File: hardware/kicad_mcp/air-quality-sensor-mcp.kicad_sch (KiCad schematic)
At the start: 16 parts, among them J1 JST_PH_2pin_Battery, U1 XIAO_ESP32C3, U2 Adafruit_SCD41, U3 Adafruit_SGP41, U4 SSD1306_OLED_128x64, U5 TP4056_USB-C_Module

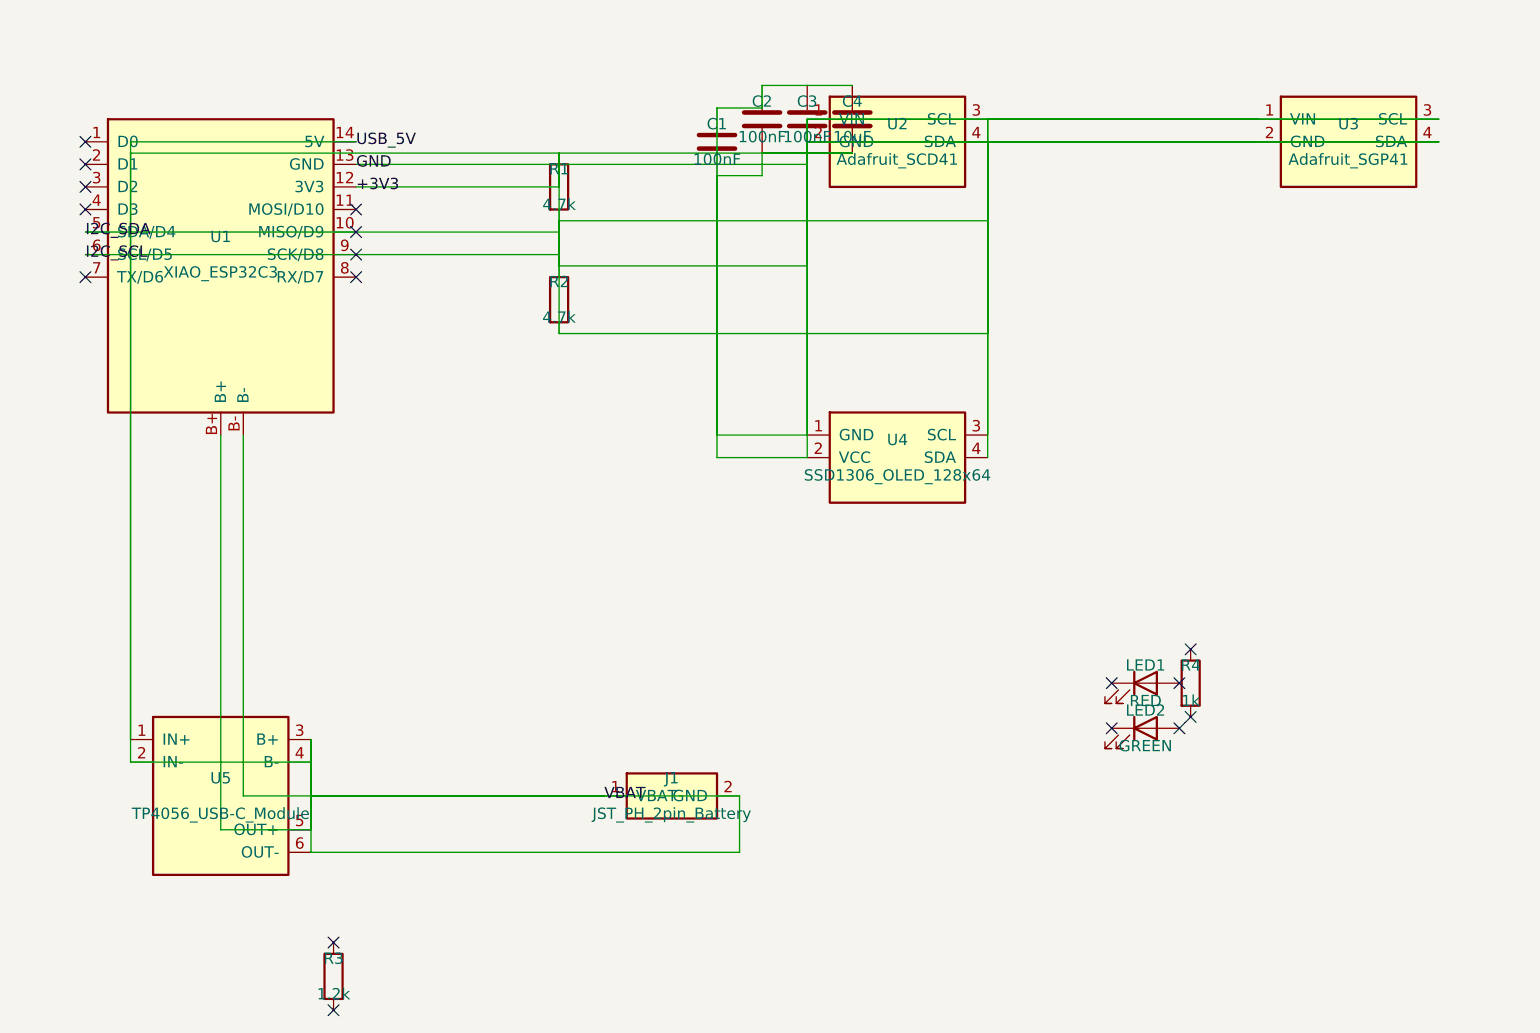
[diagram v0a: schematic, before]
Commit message: Rewire MCP schematic visibly and refresh hardware docs
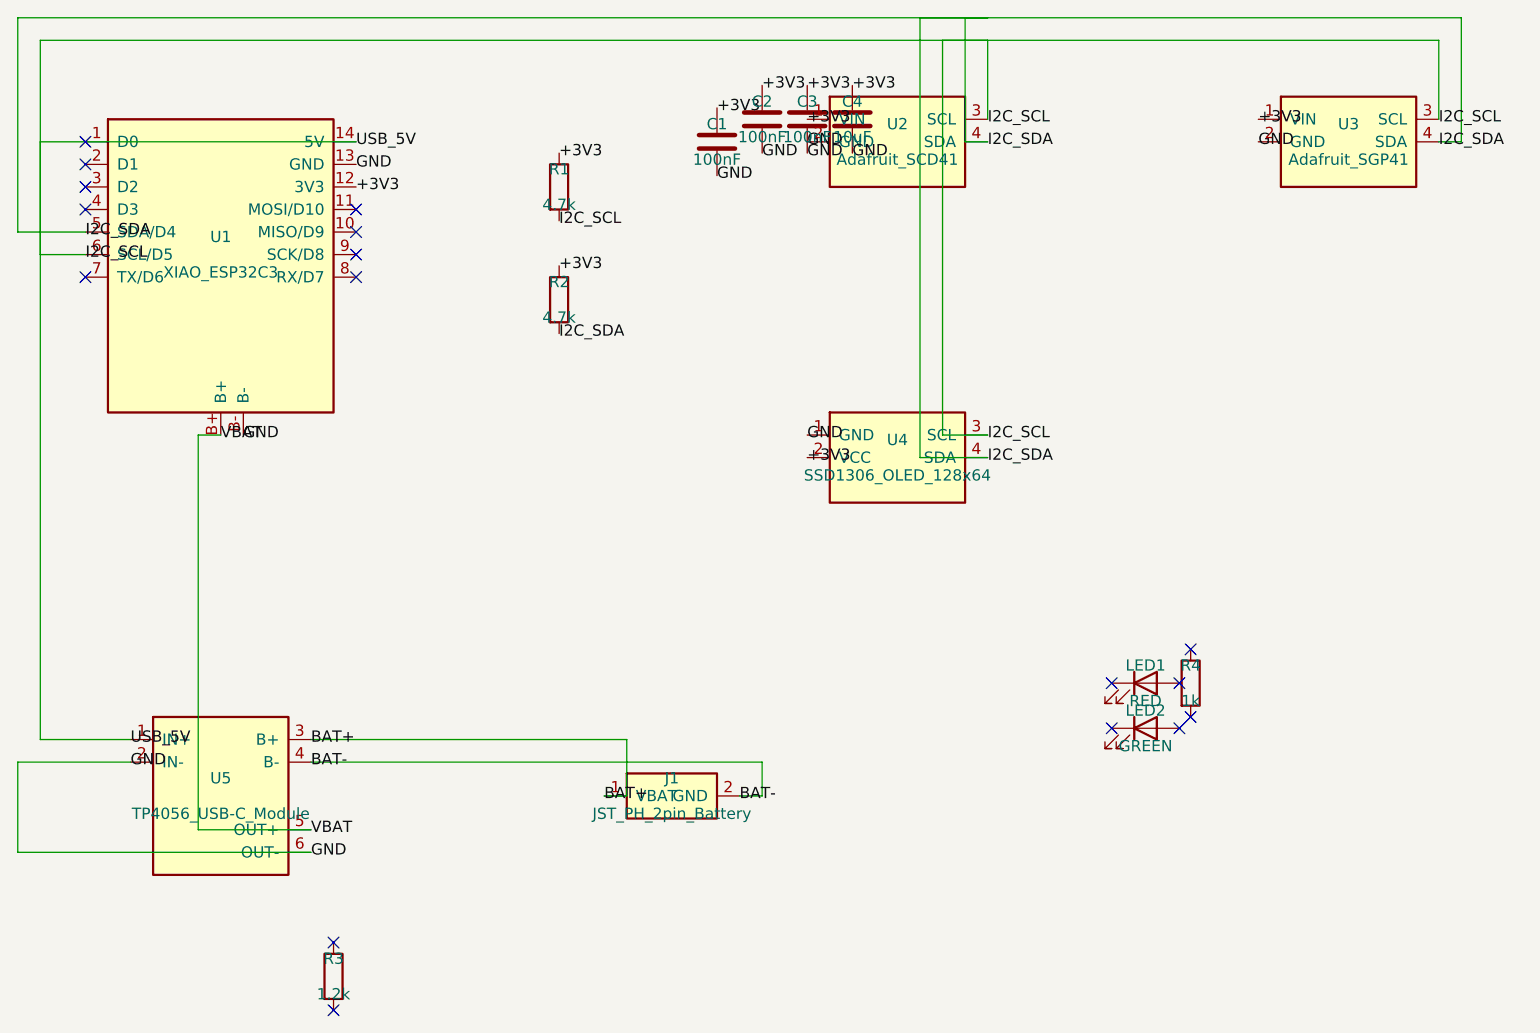
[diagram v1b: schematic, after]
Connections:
- net +3V3: no longer C1.2, C2.2, C3.2, C4.2, J1.1 (VBAT), J1.2 (GND), R1.2, R2.2, U1.13 (GND), U1.14 (5V), U1.5 (SDA/D4), U1.6 (SCL/D5), U1.B+, U1.B-, U2.2 (GND), U2.3 (SCL), U2.4 (SDA), U3.2 (GND), U3.3 (SCL), U3.4 (SDA), U4.1 (GND), U4.3 (SCL), U4.4 (SDA), U5.1 (IN+), U5.2 (IN-), U5.3 (B+), U5.4 (B-), U5.5 (OUT+), U5.6 (OUT-)
- new net BAT+: J1.1 (VBAT), U5.3 (B+)
- new net BAT-: J1.2 (GND), U5.4 (B-)
- new net GND: C1.2, C2.2, C3.2, C4.2, U1.13 (GND), U1.B-, U2.2 (GND), U3.2 (GND), U4.1 (GND), U5.2 (IN-), U5.6 (OUT-)
- new net I2C_SCL: R1.2, U1.14 (5V), U1.6 (SCL/D5), U2.3 (SCL), U3.3 (SCL), U4.3 (SCL), U5.1 (IN+)
- new net I2C_SDA: R2.2, U1.5 (SDA/D4), U2.4 (SDA), U3.4 (SDA), U4.4 (SDA)
- new net VBAT: U1.B+, U5.5 (OUT+)
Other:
- title: Wearable Air Quality Sensor (Fresh MCP Design) -> Wearable Air Quality Sensor (MCP Design)

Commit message: Finalize MCP demo board, docs, and manufacturing outputs
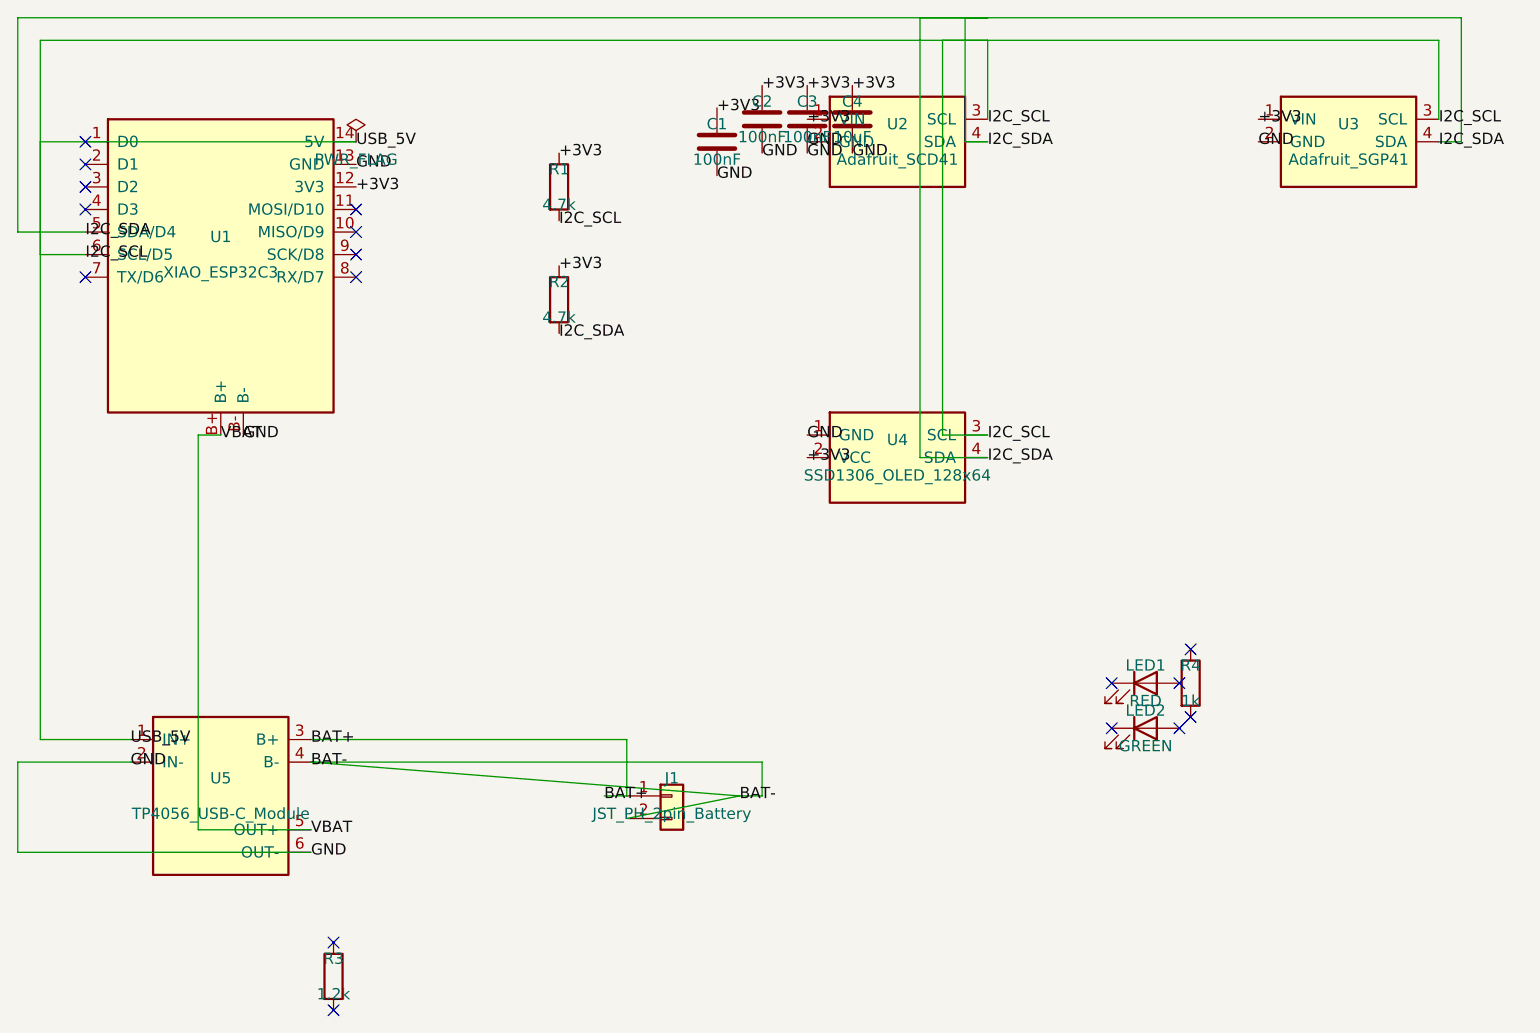
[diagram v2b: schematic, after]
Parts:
- removed J1: JST_PH_2pin_Battery, AirQuality:JST_PH_2pin_Battery, symbol AirQuality_Sensors:JST_PH_2pin
- added J1: JST_PH_2pin_Battery, AirQuality:JST_PH_2pin_Battery, symbol Connector_Generic:Conn_01x02
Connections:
- net BAT+: now also J1.1 (Pin_1)
- net BAT-: now also J1.2 (Pin_2)
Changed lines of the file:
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@@
     (rev "A")
   )
+  (wire (pts (xy 60.96 146.05) (xy 109.22 149.86))
+    (stroke (width 0) (type default))
+  )
+  (symbol (lib_id "Connector_Generic:Conn_01x02") (at 101.6 149.86 0.0) (unit 1)
+    (in_bom yes) (on_board yes) (dnp no)
+    (property "Reference" "J1" (at 101.6 147.86 0)
+      (effects (font (size 1.27 1.27)))
+    )
+    (property "Value" "JST_PH_2pin_Battery" (at 101.6 151.86 0)
+      (effects (font (size 1.27 1.27)))
+    )
+    (property "Footprint" "AirQuality:JST_PH_2pin_Battery" (at 101.6 153.86 0)
+      (effects (font (size 1.27 1.27)) hide)
+    )
+    (instances
+      (project ""
+        (path "/025eedaf-9779-457c-a85c-2ea332d6b66a"
+          (reference "J1") (unit 1)
+        )
+      )
+    )
+  )
+  (symbol (lib_id "power:PWR_FLAG") (at 66.04 76.2 0.0) (unit 1)
+    (in_bom yes) (on_board yes) (dnp no)
+    (property "Reference" "#PWR001" (at 66.04 74.2 0)
+      (effects (font (size 1.27 1.27)) hide)
+    )
+    (property "Value" "PWR_FLAG" (at 66.04 78.2 0)
+      (effects (font (size 1.27 1.27)))
+    )
+    (instances
+      (project ""
+        (path "/025eedaf-9779-457c-a85c-2ea332d6b66a"
+          (reference "#PWR001") (unit 1)
+        )
+      )
+    )
+  )
+  (no_connect (at 158.75 142.24))
   (no_connect (at 151.13 142.24))
   (no_connect (at 158.75 137.16))
@@
     )
   )
-  (symbol (lib_id "AirQuality_Sensors:JST_PH_2pin") (at 101.6 149.86 0.0) (unit 1)
-    (in_bom yes) (on_board yes) (dnp no)
-    (property "Reference" "J1" (at 101.6 147.86 0)
-      (effects (font (size 1.27 1.27)))
-    )
-    (property "Value" "JST_PH_2pin_Battery" (at 101.6 151.86 0)
-      (effects (font (size 1.27 1.27)))
-    )
-    (property "Footprint" "AirQuality:JST_PH_2pin_Battery" (at 101.6 153.86 0)
-      (effects (font (size 1.27 1.27)) hide)
-    )
-    (instances
-      (project ""
-        (path "/025eedaf-9779-457c-a85c-2ea332d6b66a"
-          (reference "J1") (unit 1)
-        )
-      )
-    )
-  )
-  (symbol (lib_id "AirQuality_Sensors:TP4056_Module") (at 50.8 149.86 0.0) (unit 1)
+(symbol (lib_id "AirQuality_Sensors:TP4056_Module") (at 50.8 149.86 0.0) (unit 1)
     (in_bom yes) (on_board yes) (dnp no)
     (property "Reference" "U5" (at 50.8 147.86 0)
